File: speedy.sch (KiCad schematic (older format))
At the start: 163 parts, among them IC1 TC4424EPA, IC3 VR, IC4 SP721, IC5 LTV827, IC7 TC4424EPA, IC8 TC4424EPA, J1 Conn_02x21_Counter_Clockwise, J2 CONN_01X26, J4 CONN_01X05, Q1 STP62NS04Z, Q10 BC547(b), Q2 STP62NS04Z, Q3 STP62NS04Z, Q4 STP62NS04Z, Q5 STP62NS04Z, Q6 STP62NS04Z, Q7 STP62NS04Z, Q8 STP62NS04Z, Q9 VP3203N3-G, U1 LD1085V50

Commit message: change vreg
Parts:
- removed U1: LD1085V50, conTE42:TO-220-LongPads, symbol LD1085V50:LD1085V50
- added U1: L4940-5V, Package_TO_SOT_THT:TO-220-3_Vertical, symbol Regulator_Linear:LM78M05_TO252
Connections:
- wire segments 398 -> 399
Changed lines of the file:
@@
 EESchema Schematic File Version 4
 LIBS:speedy-cache
-EELAYER 26 0
+EELAYER 29 0
 EELAYER END
 $Descr A4 11693 8268
@@
 GND
 $Comp
-L LD1085V50:LD1085V50 U1
-U 1 1 5AA1499A
-P 9600 6100
-F 0 "U1" H 9300 6350 50  0000 C CNN
-F 1 "LD1085V50" H 9600 6300 50  0000 C CNN
-F 2 "conTE42:TO-220-LongPads" H 9600 6200 50  0001 C CIN
-F 3 "" H 9600 6100 50  0001 C CNN
-	1    9600 6100
-	1    0    0    -1
-$EndComp
-$Comp
 L speedy-rescue:R R70
 U 1 1 5AA1C246
@@
 	1    0    0    -1
 $EndComp
-Wire Wire Line
-	10050 6050 10250 6050
 Connection ~ 10250 6050
 Connection ~ 10500 6050
@@
 	8800 6050 8950 6050
 Wire Wire Line
-	9050 6050 9150 6050
-Wire Wire Line
 	9600 6400 10050 6400
 Wire Wire Line
@@
 Connection ~ 8350 5300
 $Comp
-L power:GND #PWR?
+L power:GND #PWR0103
 U 1 1 5C9153AE
 P 7800 5800
-F 0 "#PWR?" H 7800 5550 50  0001 C CNN
+F 0 "#PWR0103" H 7800 5550 50  0001 C CNN
 F 1 "GND" H 7805 5627 50  0000 C CNN
 F 2 "" H 7800 5800 50  0001 C CNN
@@
 Wire Wire Line
 	7800 5300 8350 5300
+$Comp
+L Regulator_Linear:LM78M05_TO252 U1
+U 1 1 5C957EA1
+P 9600 6050
+F 0 "U1" H 9600 6292 50  0000 C CNN
+F 1 "L4940-5V" H 9600 6201 50  0000 C CNN
+F 2 "Package_TO_SOT_THT:TO-220-3_Vertical" H 9600 6275 50  0001 C CIN
+F 3 "http://www.fairchildsemi.com/ds/LM/LM78M05.pdf" H 9600 6000 50  0001 C CNN
+	1    9600 6050
+	1    0    0    -1
+$EndComp
+Wire Wire Line
+	9900 6050 10250 6050
+Wire Wire Line
+	9050 6050 9300 6050
+Wire Wire Line
+	9600 6350 9600 6400
 $EndSCHEMATC

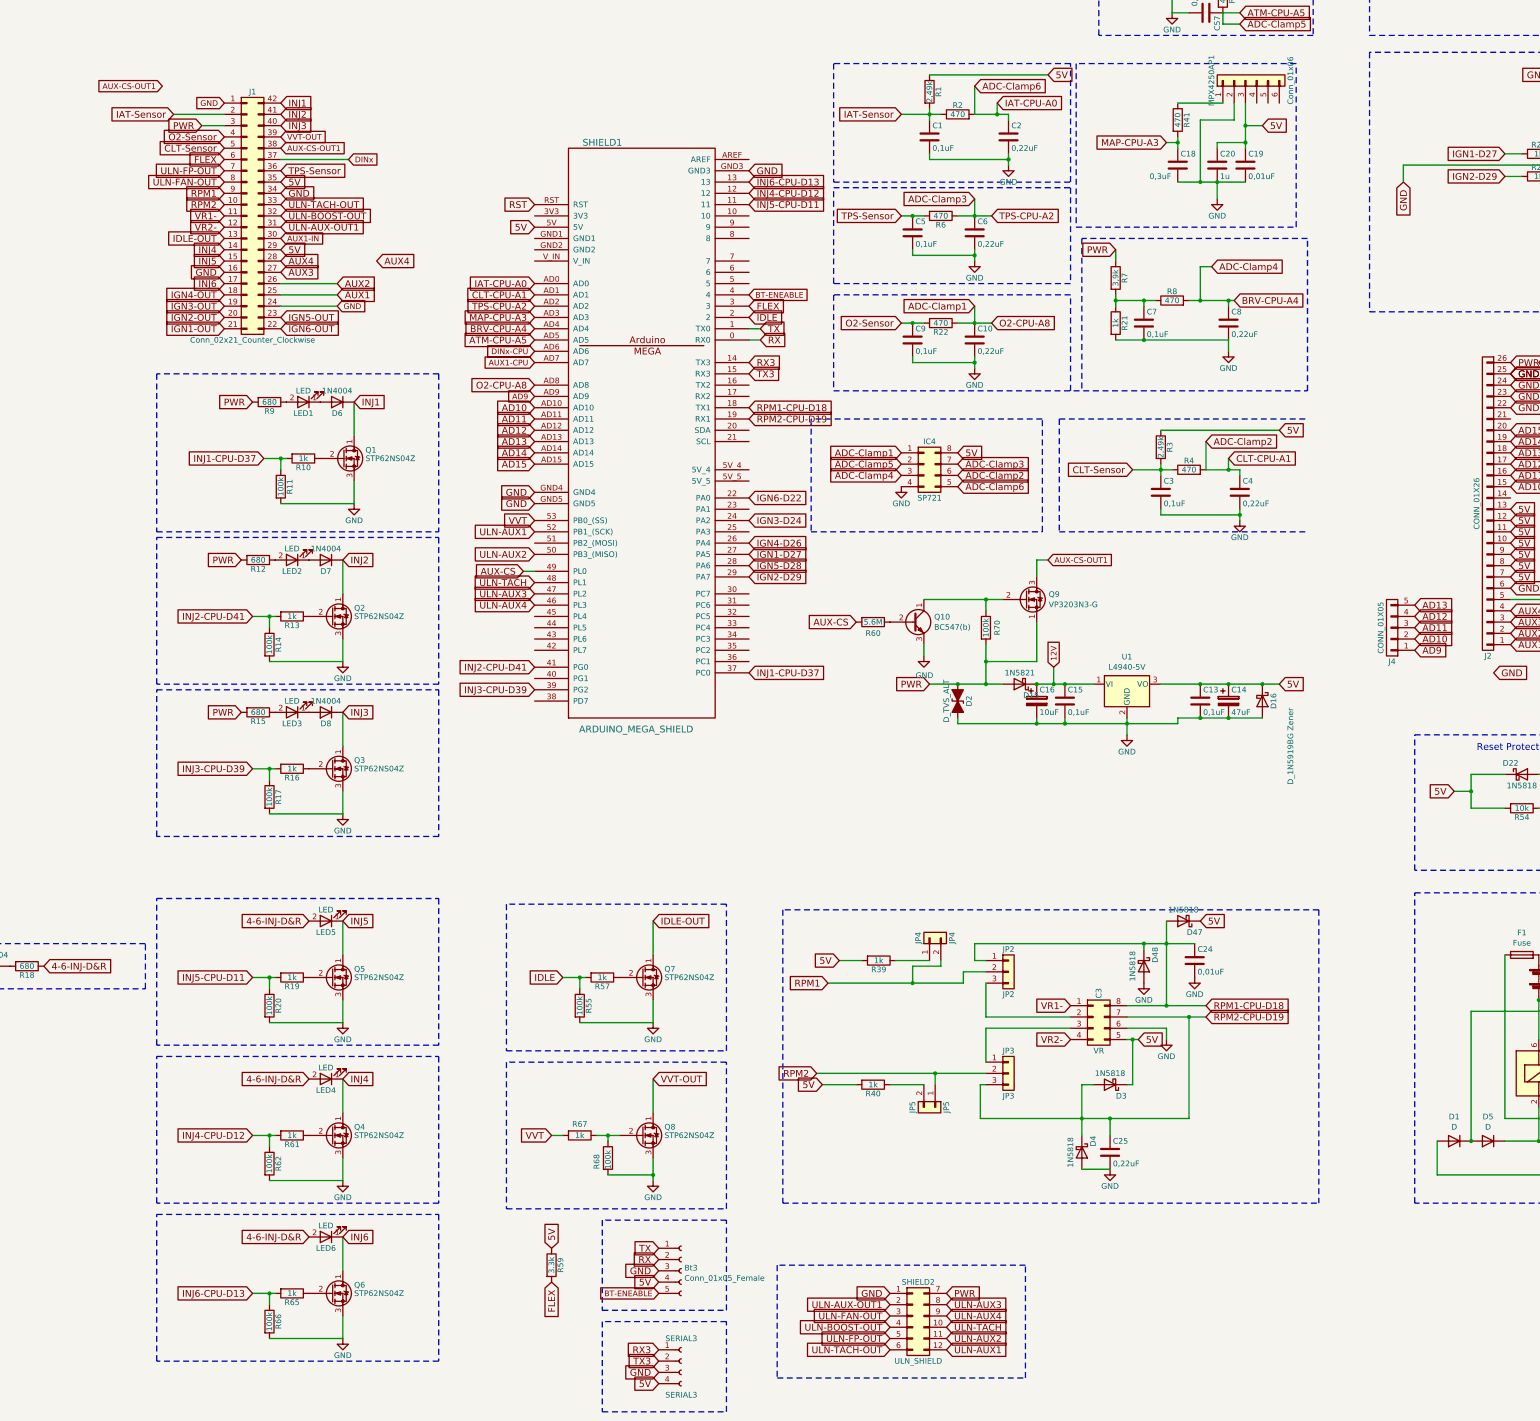
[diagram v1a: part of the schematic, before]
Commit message: Add mosfet on ULN board
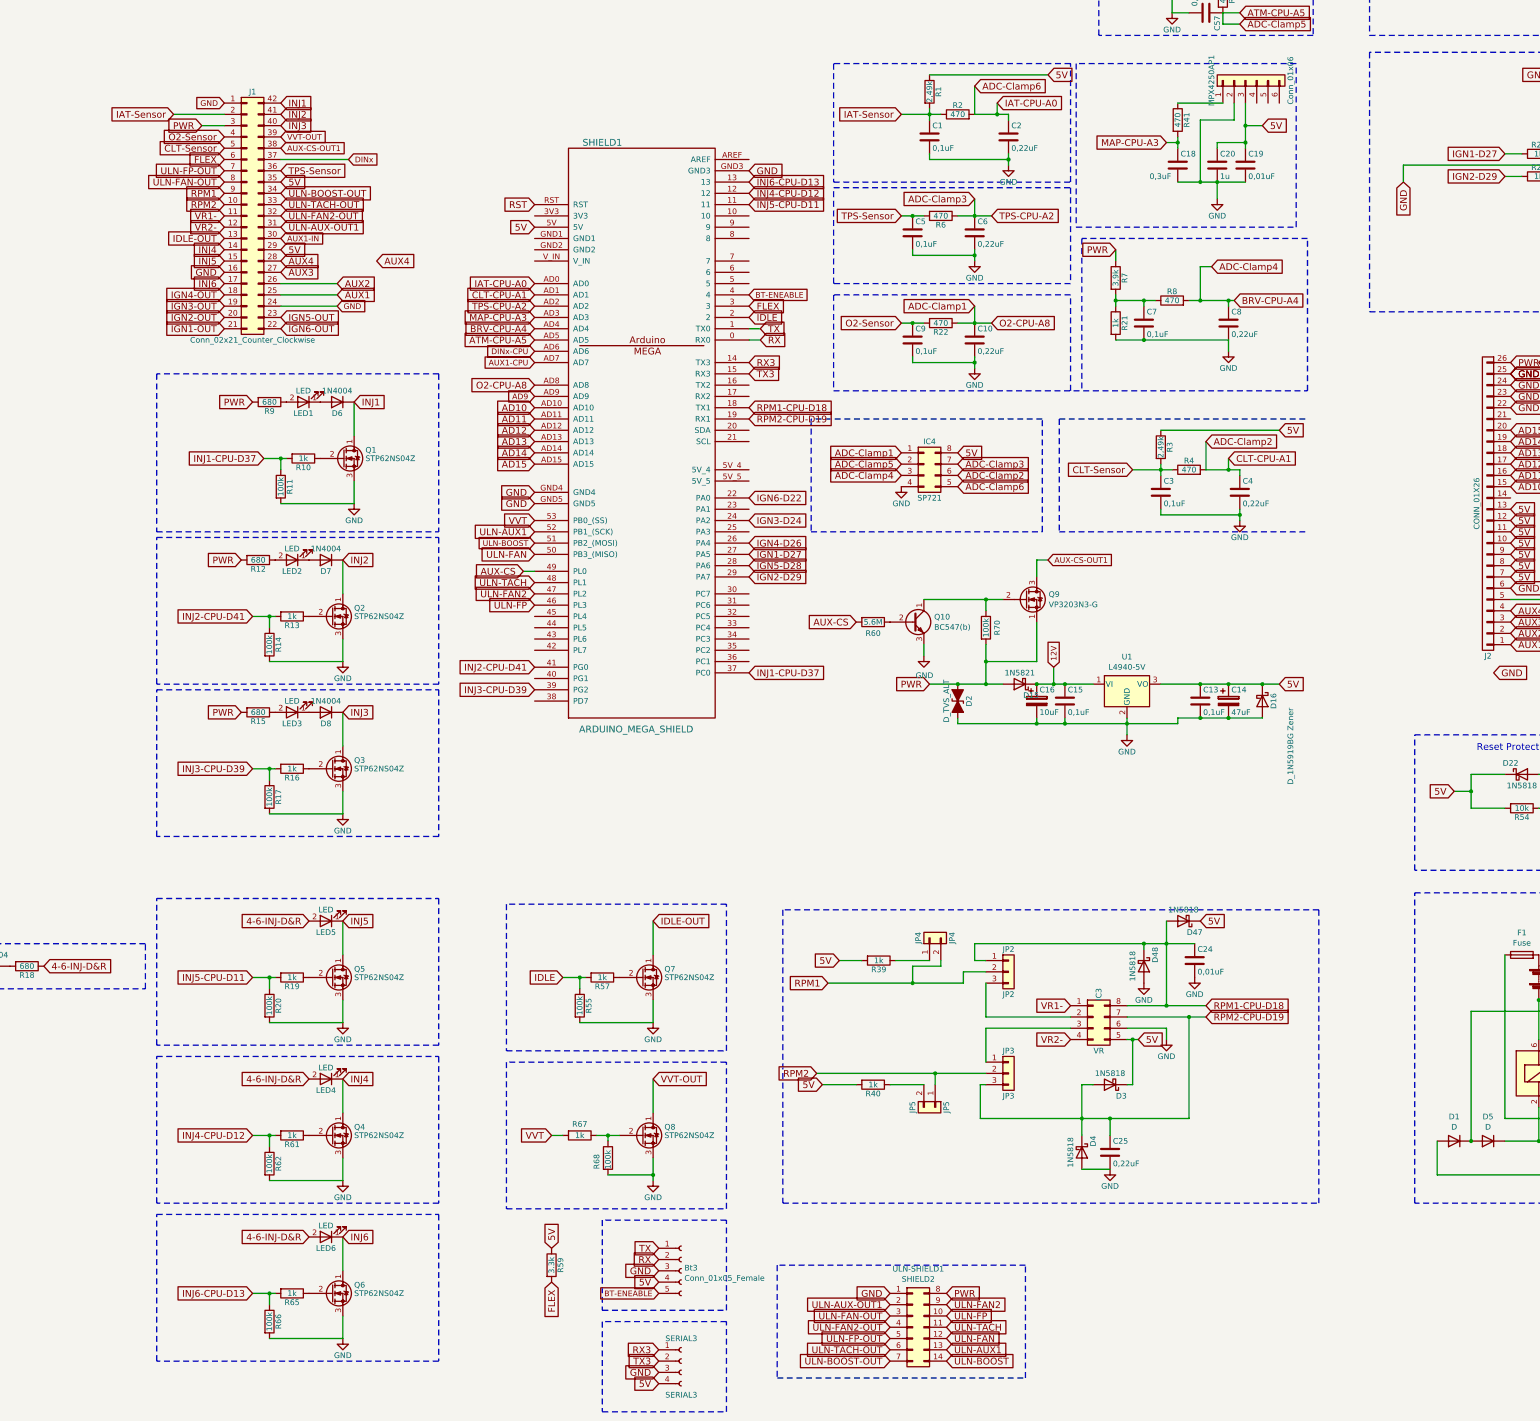
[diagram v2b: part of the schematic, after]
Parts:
- removed J4: CONN_01X05, Pin_Headers:Pin_Header_Straight_1x05_Pitch2.54mm, symbol speedy-rescue:CONN_01X05
- removed SHIELD2: ULN_SHIELD, conTE42:ULN_SHIELD, symbol speedy-rescue:Conn_02x06_Top_Bottom
- added ULN-SHIELD1: SHIELD2, conTE42:ULN_SHIELD, symbol Connector_Generic:Conn_02x07_Top_Bottom
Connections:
- net GND: now also ULN-SHIELD1.1 (Pin_1); no longer J1.34 (Pin_34)
- net PWR: now also ULN-SHIELD1.8 (Pin_8)
- net ULN-AUX-OUT1: now also ULN-SHIELD1.2 (Pin_2)
- net ULN-AUX1: now also ULN-SHIELD1.13 (Pin_13)
- net ULN-BOOST-OUT: now also J1.34 (Pin_34), ULN-SHIELD1.7 (Pin_7); no longer J1.32 (Pin_32)
- net ULN-FAN-OUT: now also ULN-SHIELD1.3 (Pin_3)
- net ULN-FP-OUT: now also ULN-SHIELD1.5 (Pin_5)
- net ULN-TACH: now also ULN-SHIELD1.11 (Pin_11)
- net ULN-TACH-OUT: now also ULN-SHIELD1.6 (Pin_6)
- net ULN-BOOST: now reaches SHIELD1.51 (PB2_(MOSI))
- net ULN-BOOST: now also ULN-SHIELD1.14 (Pin_14)
- net ULN-AUX2 renamed ULN-FAN
- net ULN-FAN: now also ULN-SHIELD1.12 (Pin_12)
- net ULN-AUX3 renamed ULN-FAN2
- net ULN-FAN2: now also ULN-SHIELD1.9 (Pin_9)
- net ULN-AUX4 renamed ULN-FP
- net ULN-FP: now also ULN-SHIELD1.10 (Pin_10)
- new net ULN-FAN2-OUT: J1.32 (Pin_32), ULN-SHIELD1.4 (Pin_4)
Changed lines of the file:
@@
 5V
 Text GLabel 2100 1700 2    60   Input ~ 0
-GND
+ULN-BOOST-OUT
 Text GLabel 6250 1800 2    60   Input ~ 0
 INJ5-CPU-D11
@@
 Text GLabel 2350 10950 0    60   Input ~ 0
 4-6-INJ-D&R
-$Comp
-L speedy-rescue:Conn_02x06_Top_Bottom SHIELD2
-U 1 1 5A5531E6
-P 7700 11650
-F 0 "SHIELD2" H 7750 11950 50  0000 C CNN
-F 1 "ULN_SHIELD" H 7750 11250 50  0000 C CNN
-F 2 "conTE42:ULN_SHIELD" H 7700 11650 50  0001 C CNN
-F 3 "" H 7700 11650 50  0001 C CNN
-	1    7700 11650
-	1    0    0    -1
-$EndComp
 Text GLabel 7500 11550 0    60   Input ~ 0
 ULN-AUX-OUT1
@@
 ULN-FP-OUT
 Text GLabel 7500 11750 0    60   Input ~ 0
-ULN-BOOST-OUT
+ULN-FAN2-OUT
 Text GLabel 7500 11450 0    60   Input ~ 0
 GND
@@
 PWR
 Text GLabel 8000 11550 2    60   Input ~ 0
-ULN-AUX3
+ULN-FAN2
 Text GLabel 8000 11650 2    60   Input ~ 0
-ULN-AUX4
+ULN-FP
 Text GLabel 8000 11850 2    60   Input ~ 0
-ULN-AUX2
+ULN-FAN
 Text GLabel 8000 11950 2    60   Input ~ 0
 ULN-AUX1
@@
 ULN-FP-OUT
 Text GLabel 2100 1900 2    60   Input ~ 0
-ULN-BOOST-OUT
+ULN-FAN2-OUT
 Text GLabel 1600 1600 0    60   Input ~ 0
 ULN-FAN-OUT
@@
 ULN-AUX1
 Text GLabel 4350 4900 0    60   Input ~ 0
-ULN-AUX2
+ULN-FAN
 Text GLabel 4350 5150 0    60   Input ~ 0
 ULN-TACH
 Text GLabel 4350 5350 0    60   Input ~ 0
-ULN-AUX4
+ULN-FP
 Text GLabel 4350 5250 0    60   Input ~ 0
-ULN-AUX3
+ULN-FAN2
 Text GLabel 6250 4900 2    60   Input ~ 0
 IGN1-D27
@@
 Text GLabel 13000 4300 2    60   Input ~ 0
 AD10
-$Comp
-L speedy-rescue:CONN_01X05 J4
-U 1 1 5AA317DB
-P 11950 5550
-F 0 "J4" H 11950 5850 50  0000 C CNN
-F 1 "CONN_01X05" V 12050 5550 50  0000 C CNN
-F 2 "Pin_Headers:Pin_Header_Straight_1x05_Pitch2.54mm" H 11950 5550 50  0001 C CNN
-F 3 "" H 11950 5550 50  0001 C CNN
-	1    11950 5550
-	-1   0    0    1
-$EndComp
-Text GLabel 12150 5350 2    60   Input ~ 0
-AD13
-Text GLabel 12150 5450 2    60   Input ~ 0
-AD12
-Text GLabel 12150 5550 2    60   Input ~ 0
-AD11
-Text GLabel 12150 5650 2    60   Input ~ 0
-AD10
-Text GLabel 12150 5750 2    60   Input ~ 0
-AD9
 Text GLabel 4350 3800 0    60   Input ~ 0
 AD12
@@
 Text GLabel 4350 3200 0    50   Input ~ 0
 AUX1-CPU
-Text GLabel 1050 750  0    50   Input ~ 0
-AUX-CS-OUT1
 Text GLabel 2100 1200 2    50   Input ~ 0
 VVT-OUT
@@
 Wire Wire Line
 	9600 6350 9600 6400
+$Comp
+L Connector_Generic:Conn_02x07_Top_Bottom ULN-SHIELD1
+U 1 1 5C977E58
+P 7700 11750
+F 0 "ULN-SHIELD1" H 7750 12267 50  0000 C CNN
+F 1 "SHIELD2" H 7750 12176 50  0000 C CNN
+F 2 "conTE42:ULN_SHIELD" H 7700 11750 50  0001 C CNN
+F 3 "~" H 7700 11750 50  0001 C CNN
+	1    7700 11750
+	1    0    0    -1
+$EndComp
+Text GLabel 7500 12050 0    60   Input ~ 0
+ULN-BOOST-OUT
+Text GLabel 8000 12050 2    60   Input ~ 0
+ULN-BOOST
+Text GLabel 4350 4800 0    50   Input ~ 0
+ULN-BOOST
 $EndSCHEMATC
